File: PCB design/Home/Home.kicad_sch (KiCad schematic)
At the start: 17 parts, among them J1 Fan, J2 LCD, J3 EM LOCK, J4 ACS712 Signal, J5 Power In, J7 RFID, J8 RFID, J9 LCD, U1 ACS712, U3 DHT11, U5 PIR, U6 MQ2

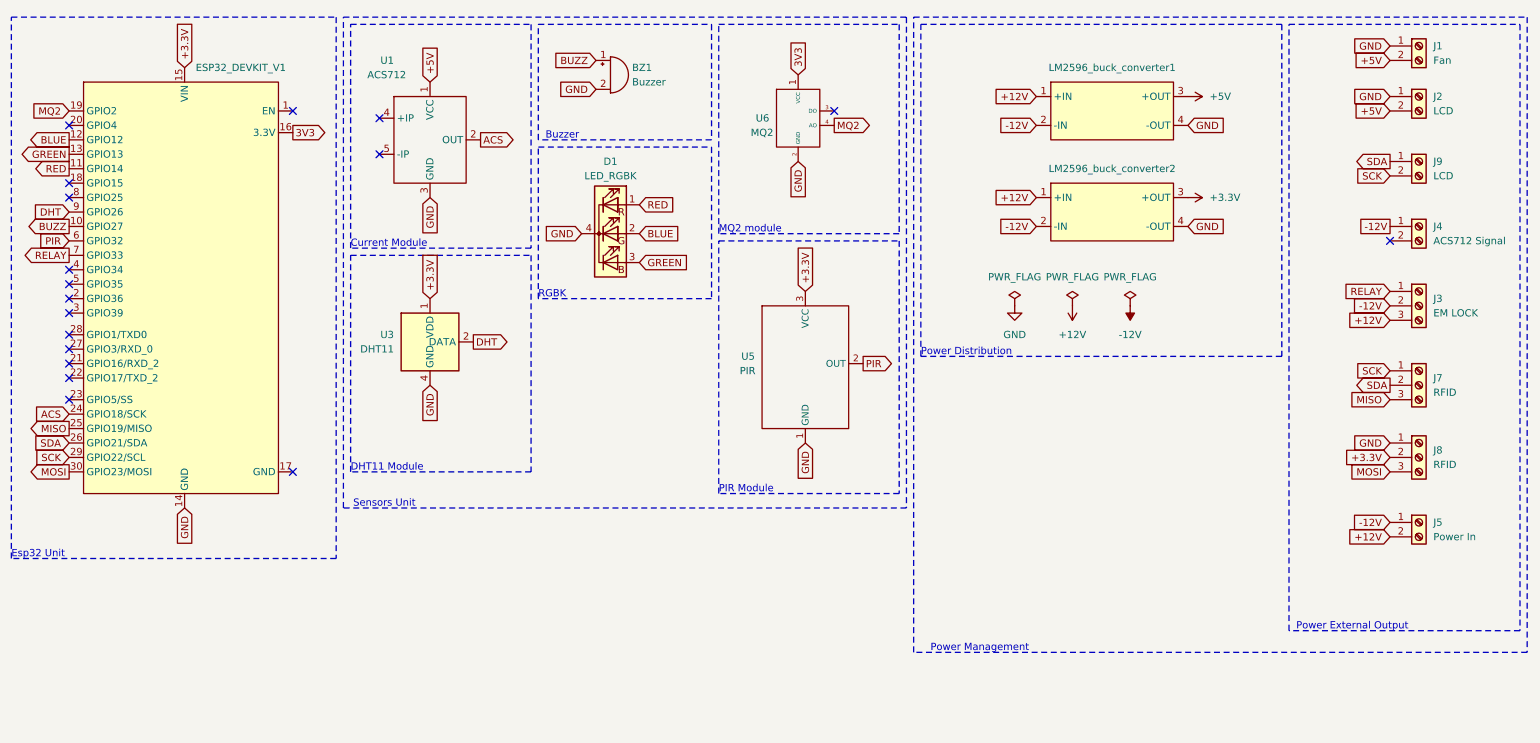
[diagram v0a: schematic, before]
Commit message: PCB rerouting, with warnings
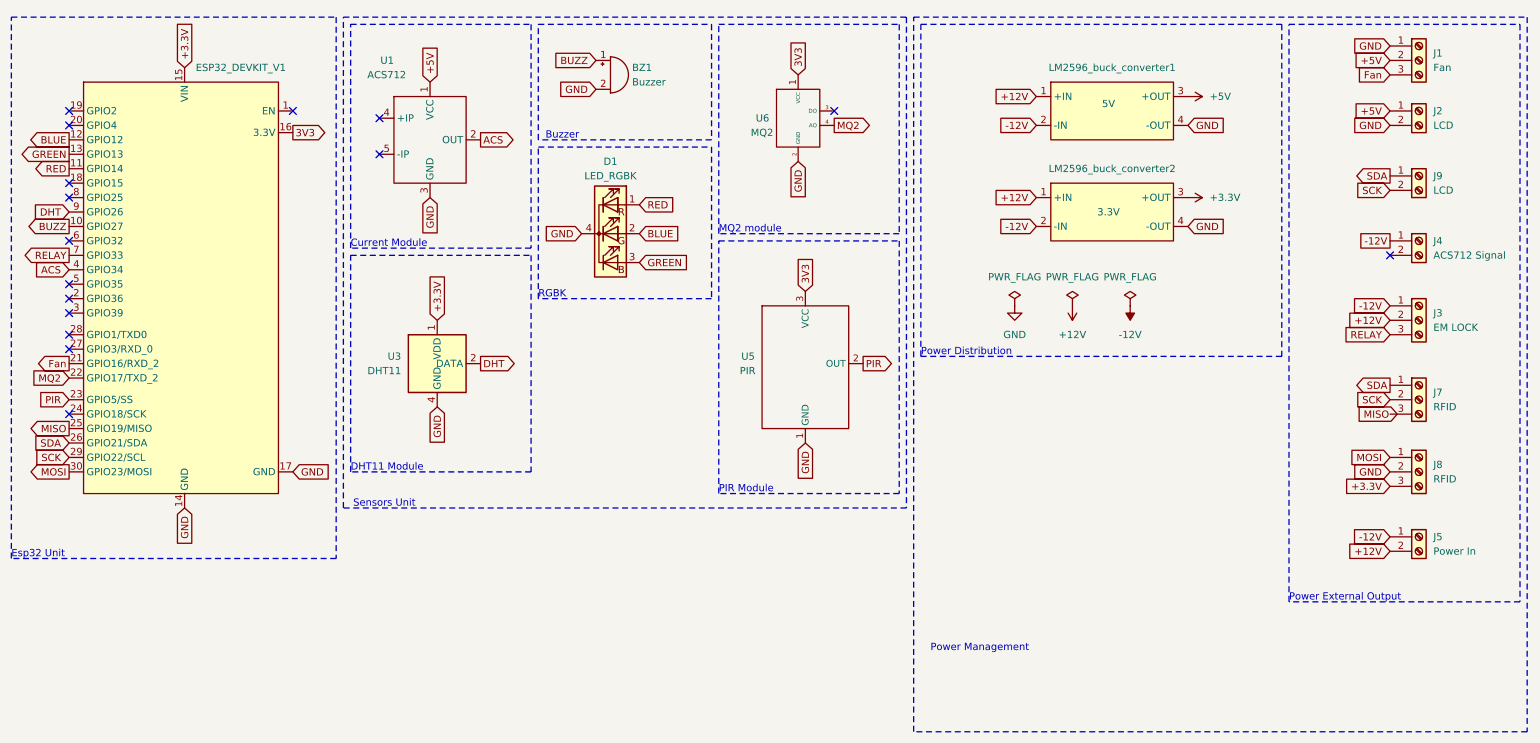
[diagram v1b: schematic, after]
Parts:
- removed J1: Fan, TerminalBlock:TerminalBlock_Altech_AK300-2_P5.00mm, symbol Connector:Screw_Terminal_01x02
- added J1: Fan, TerminalBlock:TerminalBlock_Altech_AK300-3_P5.00mm, symbol Connector:Screw_Terminal_01x03
- LM2596_buck_converter1: value ~ -> 5V
- LM2596_buck_converter2: value ~ -> 3.3V
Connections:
- net +12V: now also J3.2 (Pin_2); no longer J3.3 (Pin_3)
- net +3.3V: now also J8.3 (Pin_3); no longer J8.2 (Pin_2), U5.3 (VCC)
- net +5V: now also J2.1 (Pin_1), J1.2 (Pin_2); no longer J2.2 (Pin_2)
- net -12V: now also J3.1 (Pin_1); no longer J3.2 (Pin_2)
- net 3V3: now also U5.3 (VCC)
- net ACS: now also ESP32_DEVKIT_V1.4 (GPIO34); no longer ESP32_DEVKIT_V1.24 (GPIO18/SCK)
- net GND: now also ESP32_DEVKIT_V1.17 (GND), J2.2 (Pin_2), J8.2 (Pin_2), J1.1 (Pin_1); no longer J2.1 (Pin_1), J8.1 (Pin_1)
- net MISO: no longer J7.3 (Pin_3)
- net MOSI: now also J8.1 (Pin_1); no longer J8.3 (Pin_3)
- net MQ2: now also ESP32_DEVKIT_V1.22 (GPIO17/TXD_2); no longer ESP32_DEVKIT_V1.19 (GPIO2)
- net PIR: now also ESP32_DEVKIT_V1.23 (GPIO5/SS); no longer ESP32_DEVKIT_V1.6 (GPIO32)
- net RELAY: now also J3.3 (Pin_3); no longer J3.1 (Pin_1)
- net SCK: now also J7.2 (Pin_2); no longer J7.1 (Pin_1)
- net SDA: now also J7.1 (Pin_1); no longer J7.2 (Pin_2)
- net Fan: now reaches ESP32_DEVKIT_V1.21 (GPIO16/RXD_2)
- net Fan: now also J1.3 (Pin_3)
- no-connect marks 18 -> 16
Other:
- moved on the sheet: J2, J3, J4, J5, J7, J8, J9, U3
